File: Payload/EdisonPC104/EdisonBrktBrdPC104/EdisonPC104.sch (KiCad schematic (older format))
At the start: 22 parts, among them J17 CONN_14, J18 CONN_14, J19 CONN_14, J20 CONN_14, K3 CONN_3, P1 CONN_01X06, P2 CONN_01X06, U2 PCA9306, U3 SN74LVC1T45, U4 SN74LVC1T45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

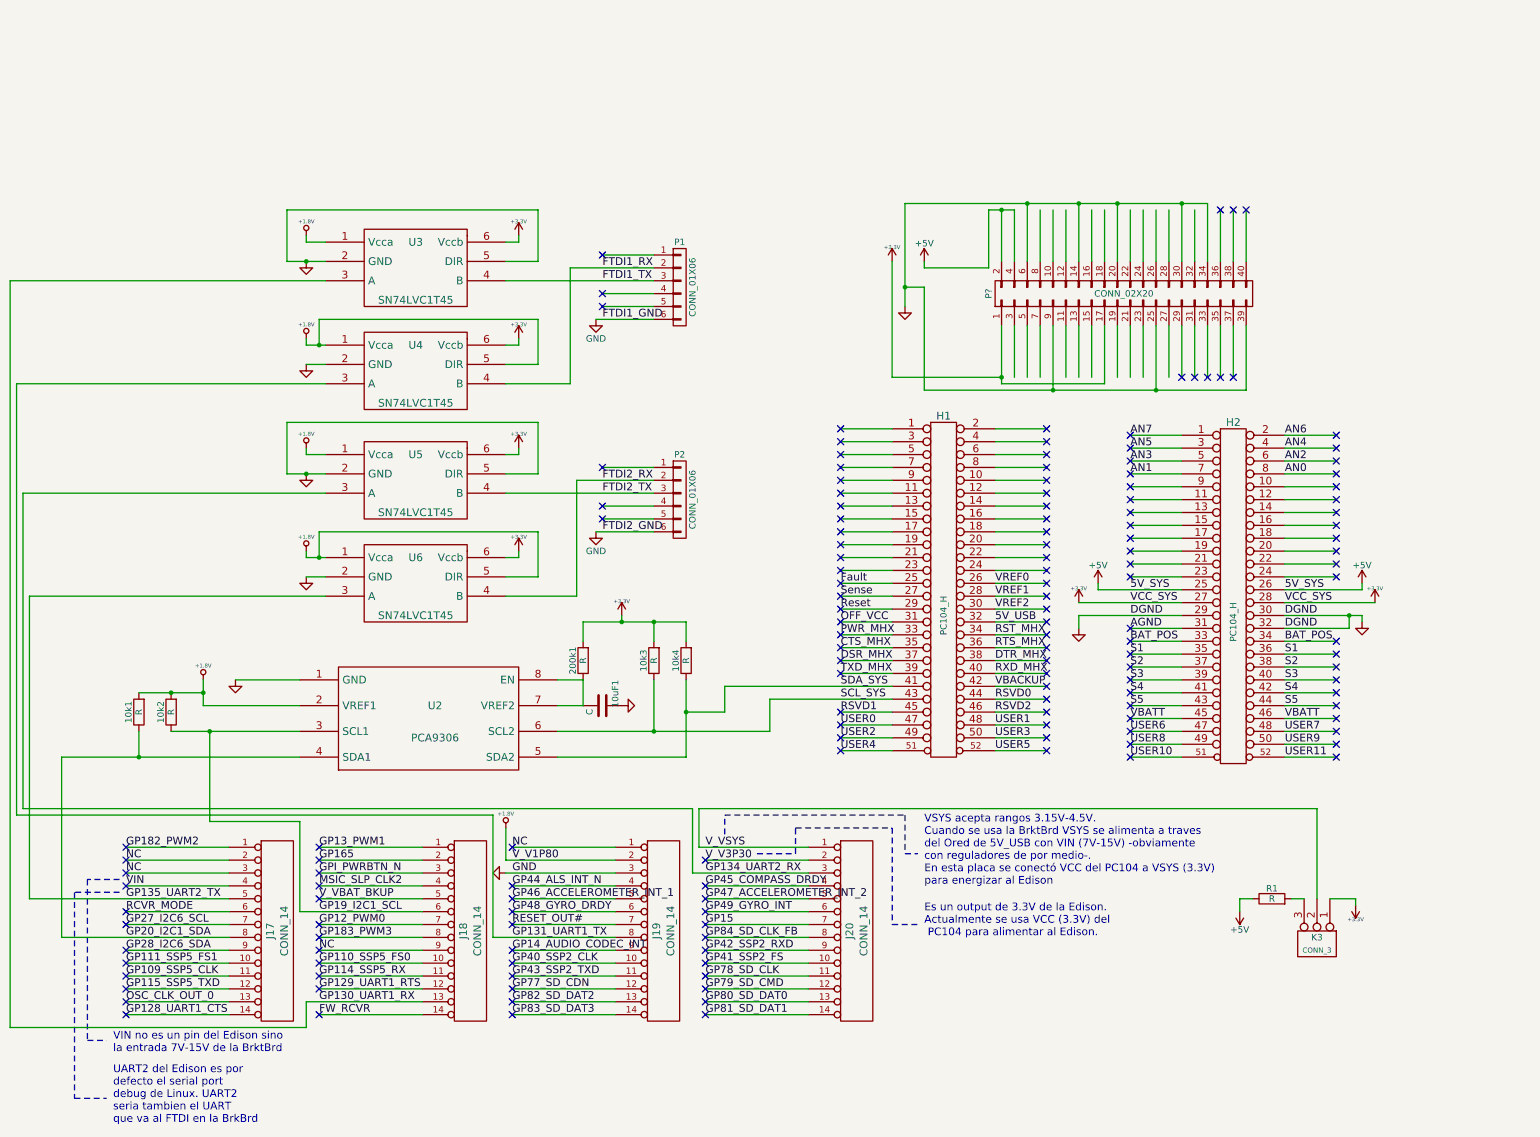
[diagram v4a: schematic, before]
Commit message: se agrega rapberry zero al PCB
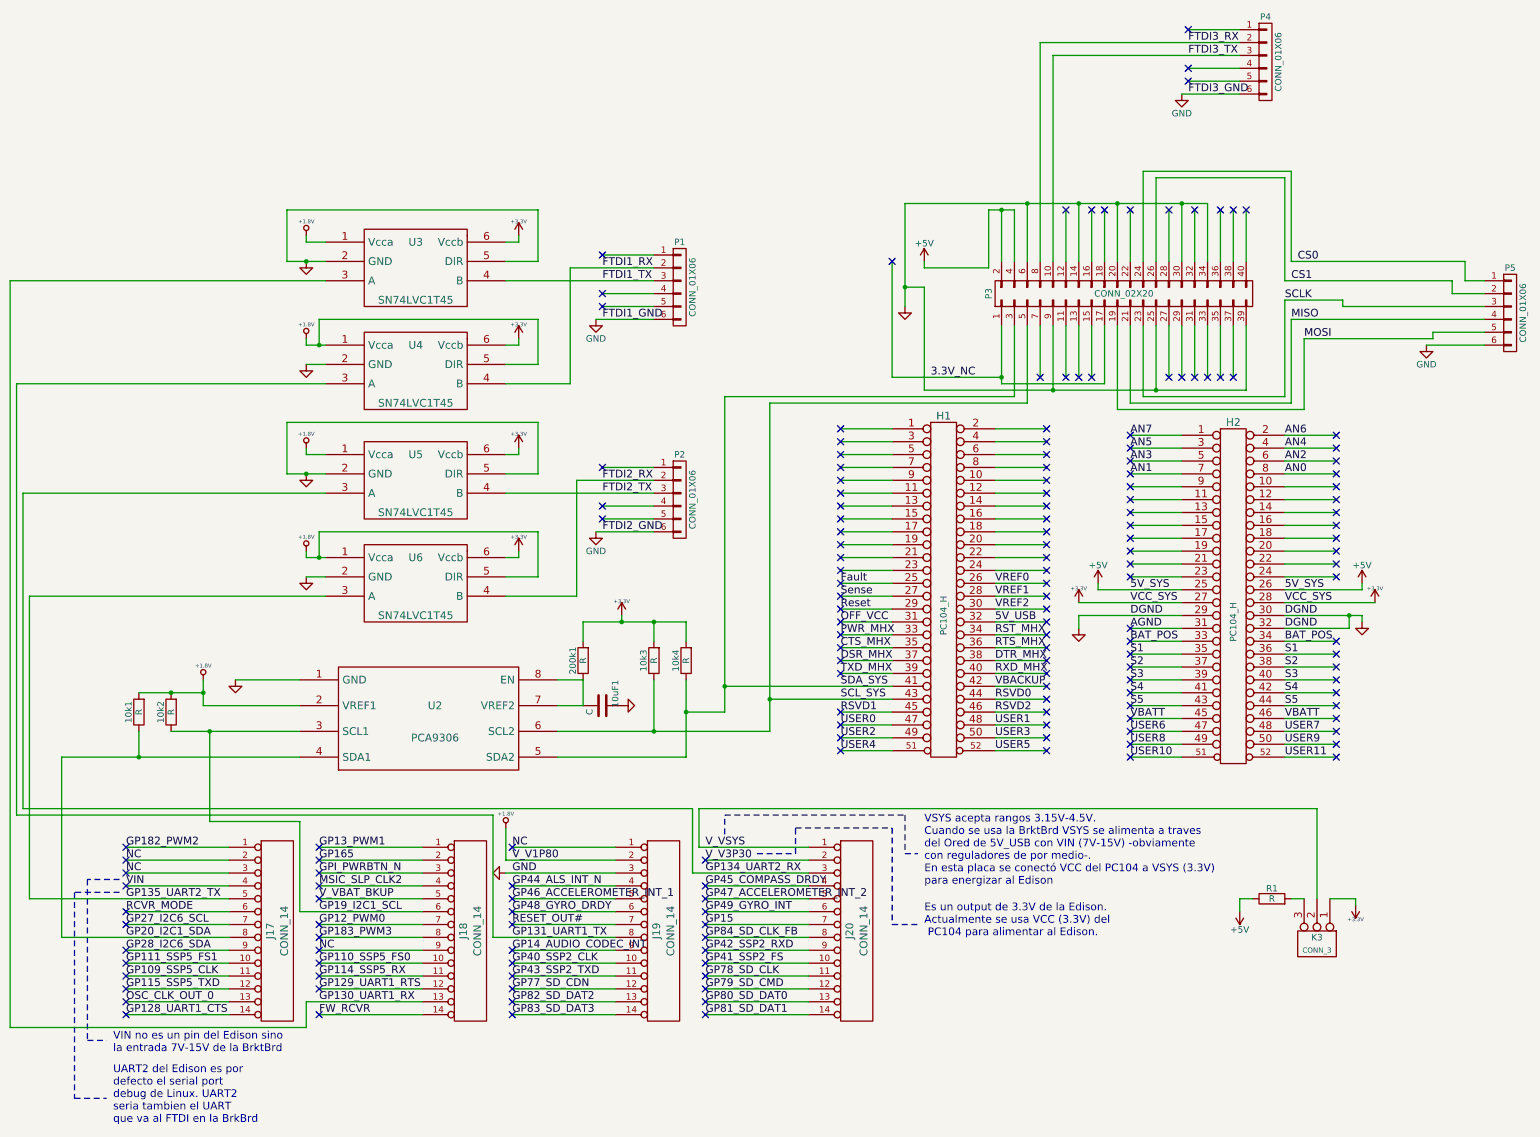
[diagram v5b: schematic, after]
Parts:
- added P4, P5: CONN_01X06, Pin_Headers:Pin_Header_Angled_1x06, symbol CONN_01X06
- P3: renamed from P?; footprint (none) -> Pin_Headers:Pin_Header_Straight_2x20
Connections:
- net labels added: 3.3V_NC, CS0, CS1, FTDI3_GND, FTDI3_RX, FTDI3_TX, MISO, MOSI, SCLK
- wire segments 318 -> 350
- no-connect marks 156 -> 171
